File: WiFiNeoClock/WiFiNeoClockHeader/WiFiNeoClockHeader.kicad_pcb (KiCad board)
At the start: 2 copper layers, 68.6 x 73.7 mm, 9 parts, among them P1 CONN_01X10, P2 CONN_01X10, P3 CONN_01X03, SW1 SW_PUSH, SW2 Switch_SPDT_x2

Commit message: Signed-off-by: Edith Li <abenoy05@gmail.com>
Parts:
- moved SW1 59.8 mm to (124.5, 61.0), turned to 90 degrees
- moved R1 57.9 mm to (121.9, 71.1)
- moved P3 41.3 mm to (154.9, 99.1), turned to 180 degrees
- moved R2 26.2 mm to (143.5, 88.9), turned to 315 degrees
- moved C1 22.9 mm to (144.8, 96.5), turned to 270 degrees
- moved P1 22.9 mm to (116.8, 101.6), turned to 180 degrees
- moved SW2 21.7 mm to (147.3, 81.3), turned to 0 degrees
- moved BT1 8.98 mm to (149.9, 73.7)
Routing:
- net VBat: track 89.6 -> 33.5 mm
- net GND: track 111.9 -> 72.0 mm
- net Net-(BT1-Pad1): track 49.1 -> 18.6 mm
- net 14: track 24.2 -> 7.40 mm
- net 15: track 44.9 -> 32.7 mm
- net Net-(P3-Pad2): track 7.62 -> 4.43 mm
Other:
- board size 68.6 x 73.7 mm -> 41.9 x 54.6 mm

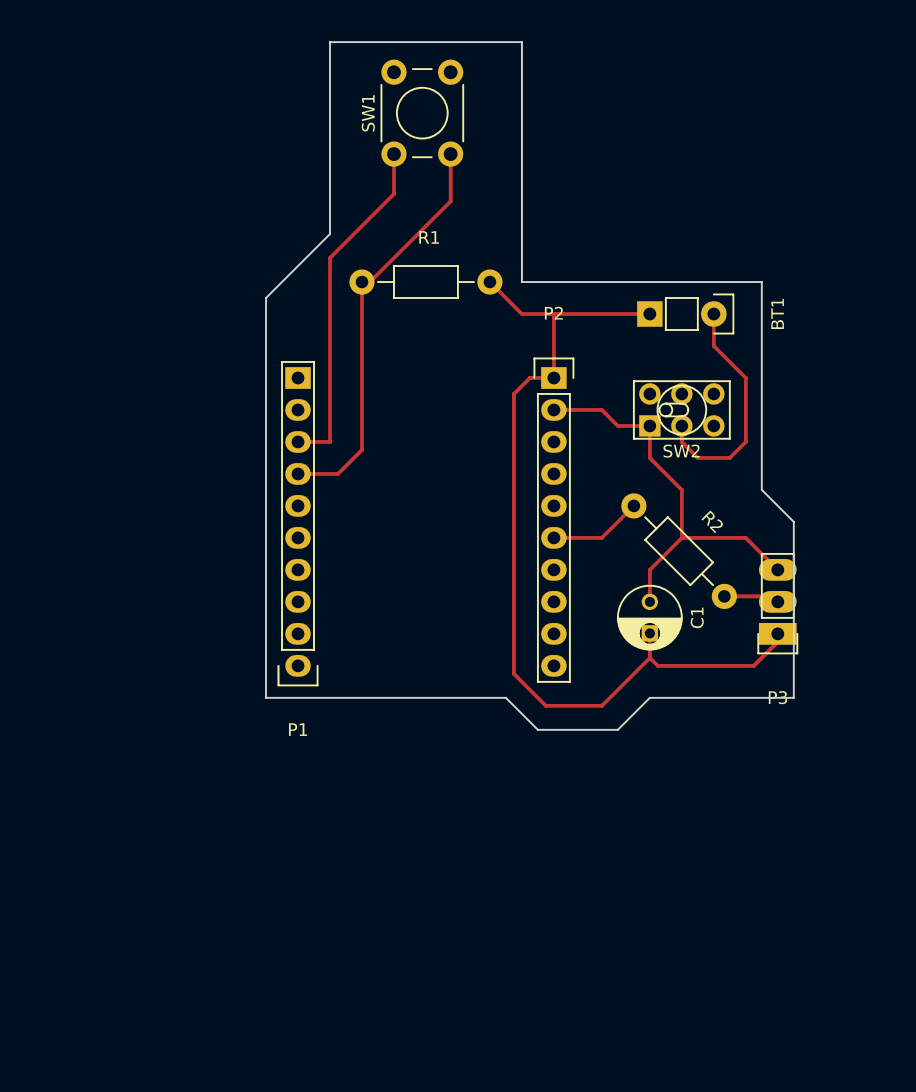
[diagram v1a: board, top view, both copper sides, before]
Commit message: updated pcb to fix milling errors
spread out the traces and fixed the drill holes for the Capacitor
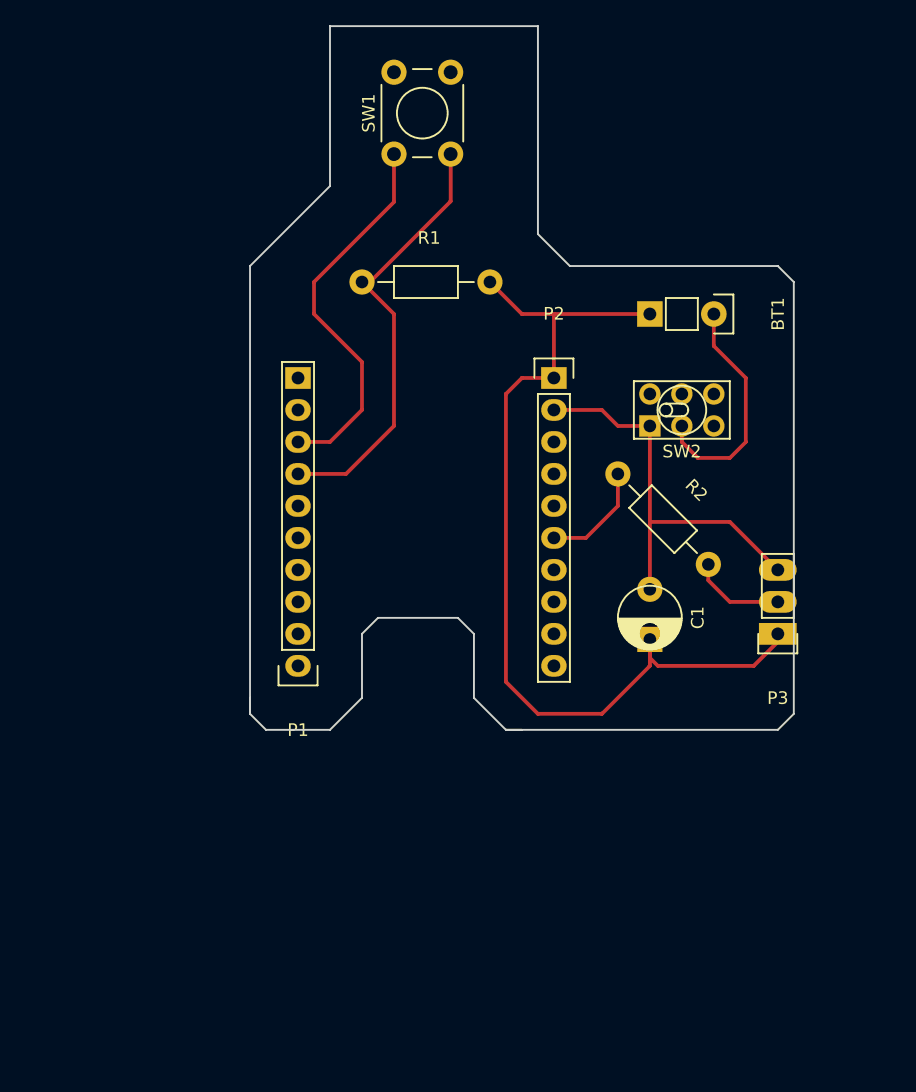
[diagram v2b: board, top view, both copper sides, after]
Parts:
- moved R2 2.84 mm to (142.2, 86.4)
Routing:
- net GND: track 72.0 -> 76.0 mm
- net Net-(P3-Pad2): track 4.43 -> 8.11 mm
- net V33: track 27.5 -> 30.7 mm
- net 15: track 32.7 -> 35.1 mm
- net 14: track 7.40 -> 8.67 mm
- net VBat: track 33.5 -> 32.9 mm
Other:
- board size 41.9 x 54.6 mm -> 43.2 x 55.9 mm
- rule trace_min: 0.2 -> 0.3

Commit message: updated kicad files with thicker traces and pads to help with soldering
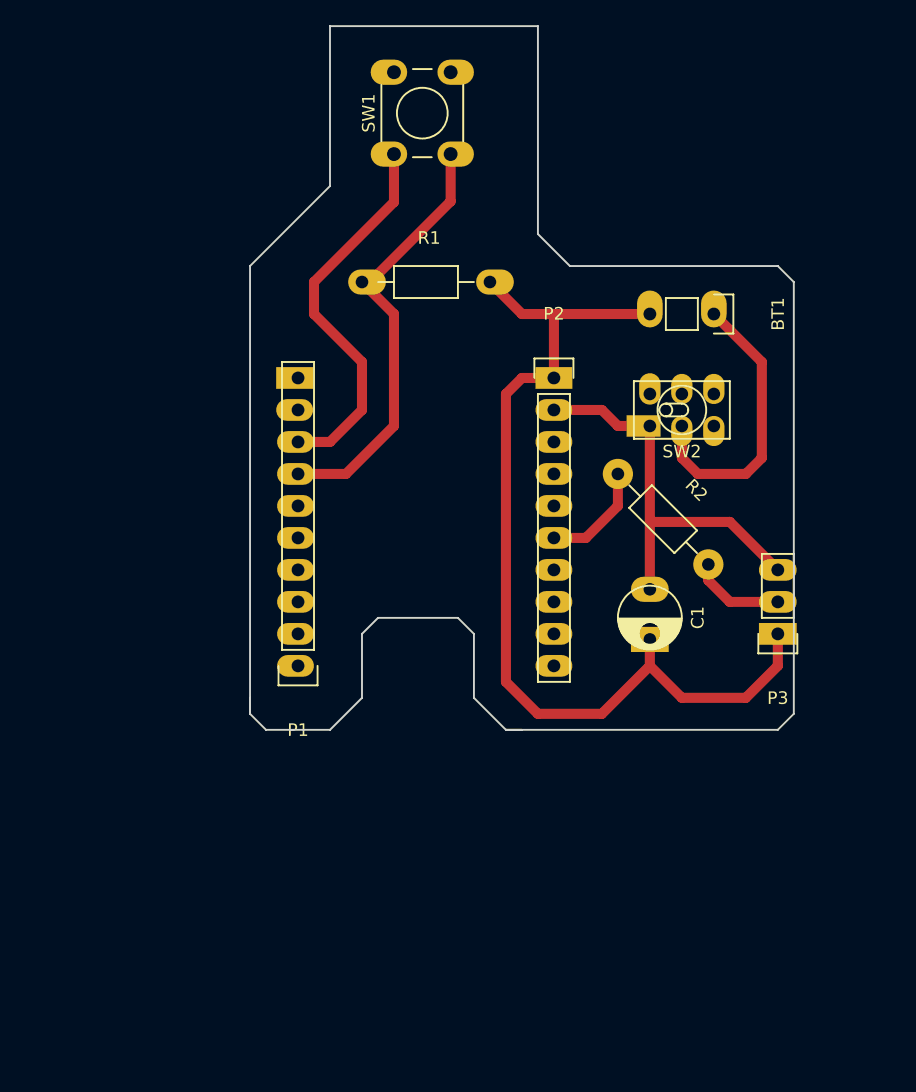
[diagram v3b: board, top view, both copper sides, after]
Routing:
- net Net-(BT1-Pad1): track 18.6 -> 23.0 mm
- net GND: track 76.0 -> 77.6 mm
